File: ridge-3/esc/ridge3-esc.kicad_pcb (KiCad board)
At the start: 6 copper layers, 36 x 36 mm, 202 parts, among them Q1AH TPN2R304PL, Q1AL TPN2R304PL, Q1BH TPN2R304PL, Q1BL TPN2R304PL, Q1CH TPN2R304PL, Q1CL TPN2R304PL, Q2AH TPN2R304PL, Q2AL TPN2R304PL, Q2BH TPN2R304PL, Q2BL TPN2R304PL, Q2CH TPN2R304PL, Q2CL TPN2R304PL, Q3AH TPN2R304PL, Q3AL TPN2R304PL, Q3BH TPN2R304PL, Q3BL TPN2R304PL, Q3CH TPN2R304PL, Q3CL TPN2R304PL, Q4AH TPN2R304PL, Q4AL TPN2R304PL, Q4BH TPN2R304PL, Q4BL TPN2R304PL, Q4CH TPN2R304PL, Q4CL TPN2R304PL

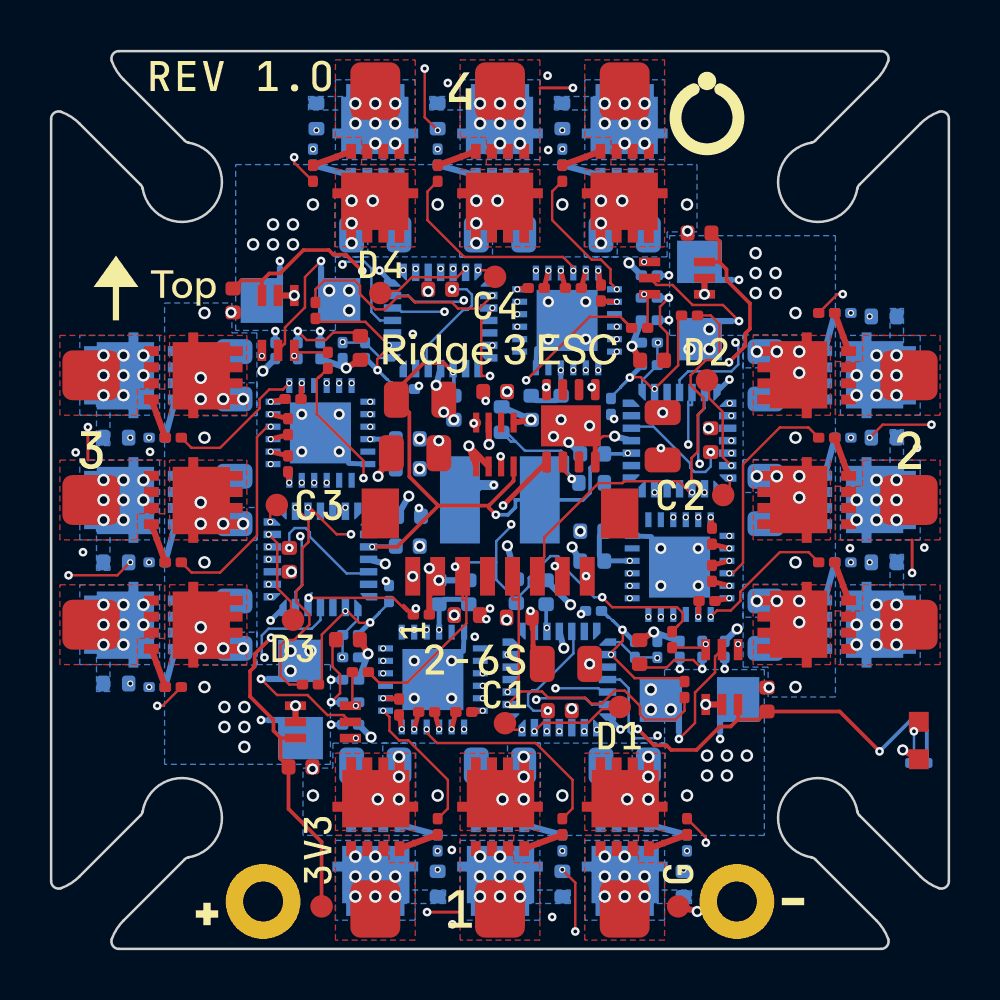
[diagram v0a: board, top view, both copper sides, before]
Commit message: ESC rev 2 routed to DRC 0/0/0 and installed
make.py --reroute esc, every gate passed: DRC 0 errors, 0 warnings,
0 unconnected; copper matches circuit.py pad for pad; BOM and CPL list
exactly the 154 assembled parts; 187 footprints == circuit.py.  8 layers
(In5/In6 gerbers new), 722 pads in the netlist.

Template channel routed with nothing open on every Freerouting variant
tried, 976 of 976 copies stamped onto the four channels, the whole-board
stage's last 4 connections repaired, clean-up from 68 dangling stubs to 0.

Co-Authored-By: Claude Opus 5.5 <noreply@anthropic.com>
Claude-Session: https://claude.ai/code/session_01MaVFAzoExts7u2gmCraXFC
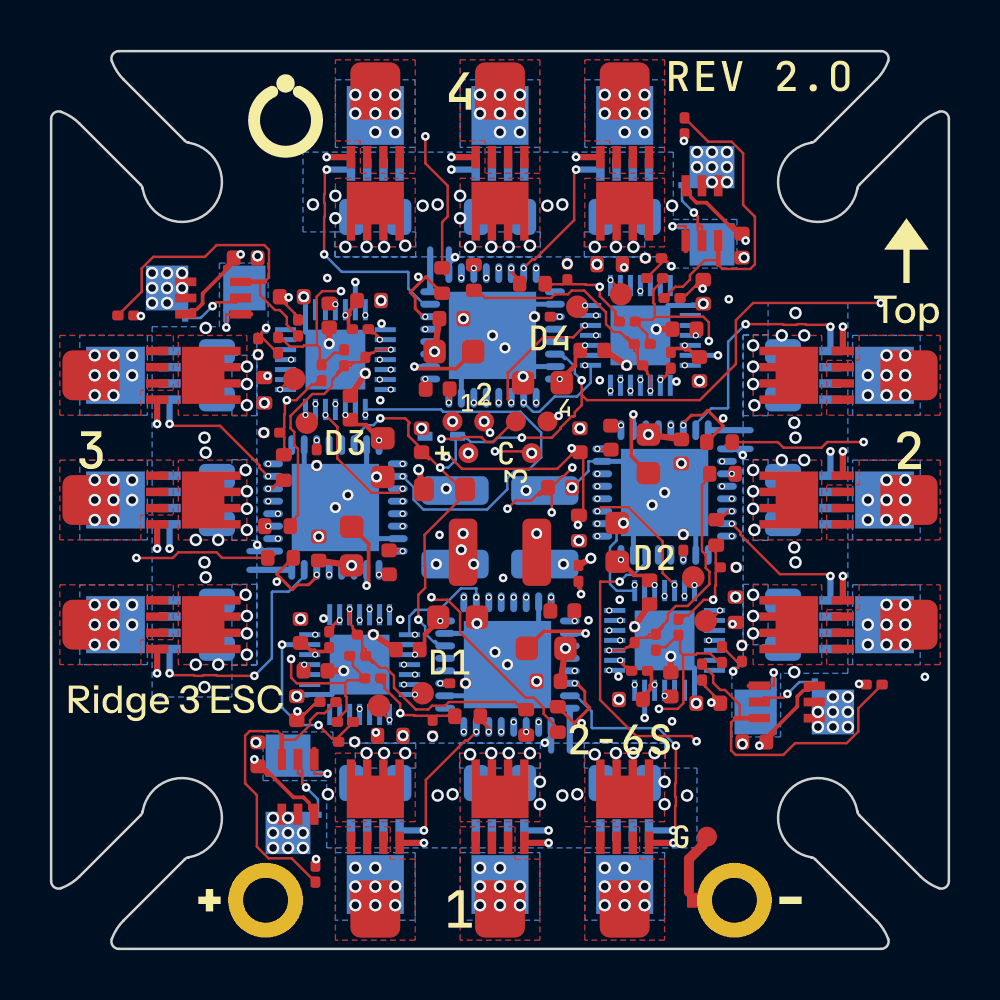
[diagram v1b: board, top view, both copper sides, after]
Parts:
- removed C55: 100nF, C_0402_1005Metric
- removed J_FC: SH-8P V, CONN-TH_BM08B-SRSS-TB-LF-SN
- removed L1: 33uH, IND-SMD_L4.0-W4.0
- removed LED_PWR: RED, LED0603-RD
- removed the P_BAT- at (109.5, 116.1)
- removed the Q1AH at (95.0, 112.3)
- removed the Q1AL at (95.0, 114.7)
- removed the Q1BH at (100.0, 112.3)
- removed the Q1BL at (100.0, 114.7)
- removed the Q1CH at (105.0, 112.3)
- removed the Q1CL at (105.0, 114.7)
- removed the Q2AH at (112.3, 105.0)
- removed the Q2AL at (114.7, 105.0)
- removed the Q2BH at (112.3, 100.0)
- removed the Q2BL at (114.7, 100.0)
- removed the Q2CH at (112.3, 95.0)
- removed the Q2CL at (114.7, 95.0)
- removed the Q3AH at (87.7, 95.0)
- removed the Q3AL at (85.3, 95.0)
- removed the Q3BH at (87.7, 100.0)
- removed the Q3BL at (85.3, 100.0)
- removed the Q3CH at (87.7, 105.0)
- removed the Q3CL at (85.3, 105.0)
- removed the Q4AH at (105.0, 87.7)
- removed the Q4AL at (105.0, 85.3)
- removed the Q4BH at (100.0, 87.7)
- removed the Q4BL at (100.0, 85.3)
- removed the Q4CH at (95.0, 87.7)
- removed the Q4CL at (95.0, 85.3)
- removed R56, R62, R67, R72: 2k, R_0201_0603Metric
- removed R57, R63, R68, R73: 10k, R_0201_0603Metric
- removed R58, R74: 1k, R_0201_0603Metric
- removed R59, R60, R64, R65, R69, R70: 10R, R_0201_0603Metric
- removed R61, R66, R71: 20k, R_0402_1005Metric
- removed TP_3V3, TP_GND: PAD_TP, PAD_TP
- removed U_BUCK: MAX15062A 3.3V, TDFN-8_L2.0-W2.0-P0.50-BL_MAX15062AATA
- removed U_GVDD: TPS7A1601, VSON-8-1EP_3x3mm_P0.65mm_EP1.65x2.4mm
- added D_EN: 4.7V, SOD-523_L1.2-W0.8-LS1.6-RD, B.Cu at (97.6, 97.4)
- added P_BAT-: PAD_BAT_K, PAD_BAT_K, F.Cu at (109.4, 116.0)
- added P_L1: PAD_LEAD, PAD_LEAD, F.Cu at (98.1, 96.8)
- added P_L2: PAD_LEAD, PAD_LEAD, F.Cu at (99.4, 96.8)
- added P_L3: PAD_LEAD, PAD_LEAD, F.Cu at (100.6, 96.8)
- added P_L4: PAD_LEAD, PAD_LEAD, F.Cu at (101.9, 96.8)
- added P_LC: PAD_LEAD, PAD_LEAD, F.Cu at (101.3, 98.1)
- added P_LG: PAD_LEAD, PAD_LEAD, F.Cu at (108.3, 113.5)
- added P_LV: PAD_LEAD, PAD_LEAD, F.Cu at (98.7, 98.1)
- added Q1AH: ISZ023N06LM6, TSDSON-8FL_L3.3-W3.3-P0.65_IFX, F.Cu at (105.0, 112.3)
- added Q1AL: ISZ023N06LM6, TSDSON-8FL_L3.3-W3.3-P0.65_IFX, B.Cu at (105.0, 114.7)
- added Q1BH: ISZ023N06LM6, TSDSON-8FL_L3.3-W3.3-P0.65_IFX, F.Cu at (100.0, 112.3)
- added Q1BL: ISZ023N06LM6, TSDSON-8FL_L3.3-W3.3-P0.65_IFX, B.Cu at (100.0, 114.7)
- added Q1CH: ISZ023N06LM6, TSDSON-8FL_L3.3-W3.3-P0.65_IFX, F.Cu at (95.0, 112.3)
- added Q1CL: ISZ023N06LM6, TSDSON-8FL_L3.3-W3.3-P0.65_IFX, B.Cu at (95.0, 114.7)
- added Q2AH: ISZ023N06LM6, TSDSON-8FL_L3.3-W3.3-P0.65_IFX, F.Cu at (112.3, 95.0)
- added Q2AL: ISZ023N06LM6, TSDSON-8FL_L3.3-W3.3-P0.65_IFX, B.Cu at (114.7, 95.0)
- added Q2BH: ISZ023N06LM6, TSDSON-8FL_L3.3-W3.3-P0.65_IFX, F.Cu at (112.3, 100.0)
- added Q2BL: ISZ023N06LM6, TSDSON-8FL_L3.3-W3.3-P0.65_IFX, B.Cu at (114.7, 100.0)
- added Q2CH: ISZ023N06LM6, TSDSON-8FL_L3.3-W3.3-P0.65_IFX, F.Cu at (112.3, 105.0)
- added Q2CL: ISZ023N06LM6, TSDSON-8FL_L3.3-W3.3-P0.65_IFX, B.Cu at (114.7, 105.0)
- added Q3AH: ISZ023N06LM6, TSDSON-8FL_L3.3-W3.3-P0.65_IFX, F.Cu at (87.7, 105.0)
- added Q3AL: ISZ023N06LM6, TSDSON-8FL_L3.3-W3.3-P0.65_IFX, B.Cu at (85.3, 105.0)
- added Q3BH: ISZ023N06LM6, TSDSON-8FL_L3.3-W3.3-P0.65_IFX, F.Cu at (87.7, 100.0)
- added Q3BL: ISZ023N06LM6, TSDSON-8FL_L3.3-W3.3-P0.65_IFX, B.Cu at (85.3, 100.0)
- added Q3CH: ISZ023N06LM6, TSDSON-8FL_L3.3-W3.3-P0.65_IFX, F.Cu at (87.7, 95.0)
- added Q3CL: ISZ023N06LM6, TSDSON-8FL_L3.3-W3.3-P0.65_IFX, B.Cu at (85.3, 95.0)
- added Q4AH: ISZ023N06LM6, TSDSON-8FL_L3.3-W3.3-P0.65_IFX, F.Cu at (95.0, 87.7)
- added Q4AL: ISZ023N06LM6, TSDSON-8FL_L3.3-W3.3-P0.65_IFX, B.Cu at (95.0, 85.3)
- added Q4BH: ISZ023N06LM6, TSDSON-8FL_L3.3-W3.3-P0.65_IFX, F.Cu at (100.0, 87.7)
- added Q4BL: ISZ023N06LM6, TSDSON-8FL_L3.3-W3.3-P0.65_IFX, B.Cu at (100.0, 85.3)
- added Q4CH: ISZ023N06LM6, TSDSON-8FL_L3.3-W3.3-P0.65_IFX, F.Cu at (105.0, 87.7)
- added Q4CL: ISZ023N06LM6, TSDSON-8FL_L3.3-W3.3-P0.65_IFX, B.Cu at (105.0, 85.3)
- added RT1: NTC 10k B3380, R_0402_1005Metric, F.Cu at (95.6, 109.5)
- added RT2: NTC 10k B3380, R_0402_1005Metric, F.Cu at (109.5, 104.4)
- added RT3: NTC 10k B3380, R_0402_1005Metric, F.Cu at (90.5, 95.6)
- added RT4: NTC 10k B3380, R_0402_1005Metric, F.Cu at (104.4, 90.5)
- C1: value 100nF -> 10uF; footprint C_0402_1005Metric -> C_1210_3225Metric; moved to F.Cu
- C10, C22, C34, C46: value 1uF -> 100nF; moved to F.Cu
- C11, C23, C35, C47: value 100nF -> 1uF; footprint C_0402_1005Metric -> C_0603_1608Metric; moved to F.Cu
- C12, C24, C36, C48: value 1uF -> 47nF; footprint C_0201_0603Metric -> C_0402_1005Metric
- C13, C25, C37, C49: value 4.7uF -> 1uF; footprint C_0805_2012Metric -> C_0603_1608Metric; moved to F.Cu
- C14, C16, C26, C28, C38, C40, C50, C52: value 1uF -> 4.7uF; footprint C_0201_0603Metric -> C_0805_2012Metric; moved to B.Cu
- C17, C29, C41, C53: value 4.7uF -> 100nF; footprint C_0805_2012Metric -> C_0402_1005Metric; moved to F.Cu
- C2: value 1uF -> 10uF; footprint C_0805_2012Metric -> C_1210_3225Metric; moved to B.Cu
- C20, C32, C44, C7, C8, R13, R14, R15, R34, R35: moved to F.Cu
- C3: value 1uF -> 10uF; footprint C_0402_1005Metric -> C_1210_3225Metric; moved to B.Cu
- C4: value 10uF -> 100nF; footprint C_0805_2012Metric -> C_0402_1005Metric
- C5: value 1uF -> 100nF; footprint C_0805_2012Metric -> C_0402_1005Metric
- C6: value 4.7uF -> 100nF; footprint C_0805_2012Metric -> C_0402_1005Metric
- R10, R52: value 10k -> 20k; footprint R_0201_0603Metric -> R_0402_1005Metric
- R11, R53: value 10R -> 2k
- R12, R44, R54: value 10R -> 10k; moved to F.Cu
- R16, R37: value 10R -> 20k; footprint R_0201_0603Metric -> R_0402_1005Metric
- R17, R38: value 10R -> 2k; moved to F.Cu
- R18, R39: value 20k -> 10k; footprint R_0402_1005Metric -> R_0201_0603Metric; moved to F.Cu
- R19: value 2k -> 1k; moved to F.Cu
- R21: value 10R -> 75k
- R22, R28, R49: value 10R -> 20k; footprint R_0201_0603Metric -> R_0402_1005Metric; moved to F.Cu
- R23, R29, R50: value 20k -> 2k; footprint R_0402_1005Metric -> R_0201_0603Metric; moved to F.Cu
- R24, R30, R51: value 2k -> 10k; moved to F.Cu
- R25: value 10k -> 20k; footprint R_0201_0603Metric -> R_0402_1005Metric; moved to F.Cu
- R26: value 1k -> 2k; moved to F.Cu
- R27, R32, R48: value 10R -> 10k
- R31: value 10k -> 1k; moved to F.Cu
- R33: value 10R -> 75k; moved to F.Cu
- R40, R46: value 2k -> 20k; footprint R_0201_0603Metric -> R_0402_1005Metric; moved to F.Cu
- R41, R47: value 10k -> 2k; moved to F.Cu
- R42: value 1k -> 10k; moved to F.Cu
- R43: value 10R -> 1k
- R45: value 20k -> 75k; footprint R_0402_1005Metric -> R_0201_0603Metric; moved to F.Cu
- R5: value 1k -> 33k; footprint R_0201_0603Metric -> R_0603_1608Metric; moved to F.Cu
- R55: value 20k -> 1k; footprint R_0402_1005Metric -> R_0201_0603Metric; moved to F.Cu
- R6: value 22R -> 100k
- R7: value 88.7k -> 10k; footprint R_0402_1005Metric -> R_0201_0603Metric; moved to F.Cu
- R8: value 10.2k -> 10k; footprint R_0402_1005Metric -> R_0201_0603Metric; moved to F.Cu
- R9: value 100k -> 75k; footprint R_0402_1005Metric -> R_0201_0603Metric
- U_ESC1, U_ESC2, U_ESC3, U_ESC4: value STM32G071GBU6 -> AT32F421G8U7; footprint UFQFPN-28_L4.0-W4.0-P0.50-BL -> QFN-28_L4.0-W4.0-P0.40-TL-EP2.4
- U_GD1, U_GD2, U_GD3, U_GD4: value DRV8300DRGER -> DRV8320H; footprint VQFN-24_L4.0-W4.0-P0.50-TL-EP2.5 -> QFN-32_L5.0-W5.0-P0.50-TL-EP3.5
- moved R55 27.1 mm to (106.9, 91.9)
- moved R34 24.7 mm to (91.2, 102.3)
- moved R54 23.9 mm to (105.1, 92.8)
- moved R37 23.6 mm to (91.1, 101.0)
- moved R53 23.0 mm to (102.7, 90.8), turned to 90 degrees
- moved R48 22.4 mm to (106.2, 91.1), turned to 0 degrees
- moved R50 22.2 mm to (105.4, 94.6), turned to 180 degrees
- moved R5 22.0 mm to (97.8, 99.6), turned to 0 degrees
- moved R39 21.7 mm to (93.8, 94.3), turned to 90 degrees
- moved R33 21.1 mm to (92.7, 98.3), turned to -90 degrees
- moved R44 20.8 mm to (106.8, 94.4), turned to -90 degrees
- moved R38 19.3 mm to (94.6, 94.6), turned to -90 degrees
- moved R51 19.2 mm to (105.7, 93.8)
- moved R32 19.2 mm to (94.4, 93.2)
- moved C18 18.9 mm to (91.8, 108.3)
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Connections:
- C1 pad 1: CUR -> VBAT
- C10 pad 1: GVDD -> VBAT
- C11 pad 1: GVDD -> M1_VCP
- C11 pad 2: GND -> VBAT
- C12 pad 1: M1_BSTA -> M1_CPH
- C12 pad 2: M1_A -> M1_CPL
- C13 pad 1: VBAT -> M1_DVDD
- C13 pad 2: M1_SRC -> GND
- C14 pad 1: M1_BSTB -> VBAT
- C14 pad 2: M1_B -> M1_SRC
- C16 pad 1: M1_BSTC -> VBAT
- C16 pad 2: M1_C -> M1_SRC
- C17 pad 1: VBAT -> M1_DVDD
- C17 pad 2: M1_SRC -> GND
- C18 pad 1: +3V3 -> M1_ISENSE
- C19 pad 1: M1_ISENSE -> M2_DVDD
- C20 pad 1: +3V3 -> M2_DVDD
- C22 pad 1: GVDD -> VBAT
- C23 pad 1: GVDD -> M2_VCP
- C23 pad 2: GND -> VBAT
- C24 pad 1: M2_BSTA -> M2_CPH
- C24 pad 2: M2_A -> M2_CPL
- C25 pad 1: VBAT -> M2_DVDD
- C25 pad 2: M2_SRC -> GND
- C26 pad 1: M2_BSTB -> VBAT
- C26 pad 2: M2_B -> M2_SRC
- C28 pad 1: M2_BSTC -> VBAT
- C28 pad 2: M2_C -> M2_SRC
- C29 pad 1: VBAT -> M2_DVDD
- C29 pad 2: M2_SRC -> GND
- C3 pad 1: BUCK_VCC -> VBAT
- C30 pad 1: +3V3 -> M2_ISENSE
- C31 pad 1: M2_ISENSE -> M3_DVDD
- C32 pad 1: +3V3 -> M3_DVDD
- C34 pad 1: GVDD -> VBAT
- C35 pad 1: GVDD -> M3_VCP
- C35 pad 2: GND -> VBAT
- C36 pad 1: M3_BSTA -> M3_CPH
- C36 pad 2: M3_A -> M3_CPL
- C37 pad 1: VBAT -> M3_DVDD
- C37 pad 2: M3_SRC -> GND
- C38 pad 1: M3_BSTB -> VBAT
- C38 pad 2: M3_B -> M3_SRC
- C4 pad 1: +3V3 -> CUR
- C40 pad 1: M3_BSTC -> VBAT
- C40 pad 2: M3_C -> M3_SRC
- C41 pad 1: VBAT -> M3_DVDD
- C41 pad 2: M3_SRC -> GND
- C42 pad 1: +3V3 -> M3_ISENSE
- C43 pad 1: M3_ISENSE -> M4_DVDD
- C44 pad 1: +3V3 -> M4_DVDD
- C46 pad 1: GVDD -> VBAT
- C47 pad 1: GVDD -> M4_VCP
- C47 pad 2: GND -> VBAT
- C48 pad 1: M4_BSTA -> M4_CPH
- C48 pad 2: M4_A -> M4_CPL
- C49 pad 1: VBAT -> M4_DVDD
- C49 pad 2: M4_SRC -> GND
- C5 pad 1: GVDD_IN -> DRV_EN
- C50 pad 1: M4_BSTB -> VBAT
- C50 pad 2: M4_B -> M4_SRC
- C52 pad 1: M4_BSTC -> VBAT
- C52 pad 2: M4_C -> M4_SRC
- C53 pad 1: VBAT -> M4_DVDD
- C53 pad 2: M4_SRC -> GND
- C54 pad 1: +3V3 -> M4_ISENSE
- C6 pad 1: GVDD -> ESC_VSENSE
- C7 pad 1: ESC_VSENSE -> M1_DVDD
- C8 pad 1: +3V3 -> M1_DVDD
- R10 pad 1: ESC_VSENSE -> M1_A
- R10 pad 2: GND -> M1_CMP_A
- R11 pad 1: M1_GHA_D -> M1_CMP_A
- R11 pad 2: M1_GHA -> GND
- R12 pad 1: M1_GLA_D -> M1_CMP_A
- R12 pad 2: M1_GLA -> M1_NEUTRAL
- R13 pad 1: M1_A -> M1_B
- R13 pad 2: M1_CMP_A -> M1_CMP_B
- R14 pad 1: M1_CMP_A -> M1_CMP_B
- R15 pad 1: M1_CMP_A -> M1_CMP_B
- R16 pad 1: M1_GHB_D -> M1_C
- R16 pad 2: M1_GHB -> M1_CMP_C
- R17 pad 1: M1_GLB_D -> M1_CMP_C
- R17 pad 2: M1_GLB -> GND
- R18 pad 1: M1_B -> M1_CMP_C
- R18 pad 2: M1_CMP_B -> M1_NEUTRAL
- R19 pad 1: M1_CMP_B -> M1_IOUT
- R19 pad 2: GND -> M1_ISENSE
- R20 pad 1: M1_CMP_B -> M2_DVDD
- R20 pad 2: M1_NEUTRAL -> M2_NTC
- R21 pad 1: M1_GHC_D -> M2_IDRIVE
- R21 pad 2: M1_GHC -> GND
- R22 pad 1: M1_GLC_D -> M2_A
- R22 pad 2: M1_GLC -> M2_CMP_A
- R23 pad 1: M1_C -> M2_CMP_A
- R23 pad 2: M1_CMP_C -> GND
- R24 pad 1: M1_CMP_C -> M2_CMP_A
- R24 pad 2: GND -> M2_NEUTRAL
- R25 pad 1: M1_CMP_C -> M2_B
- R25 pad 2: M1_NEUTRAL -> M2_CMP_B
- R26 pad 1: M1_IOUT -> M2_CMP_B
- R26 pad 2: M1_ISENSE -> GND
- R27 pad 1: M2_GHA_D -> M2_CMP_B
- R27 pad 2: M2_GHA -> M2_NEUTRAL
- R28 pad 1: M2_GLA_D -> M2_C
- R28 pad 2: M2_GLA -> M2_CMP_C
- R29 pad 1: M2_A -> M2_CMP_C
- R29 pad 2: M2_CMP_A -> GND
- R30 pad 1: M2_CMP_A -> M2_CMP_C
- R30 pad 2: GND -> M2_NEUTRAL
- R31 pad 1: M2_CMP_A -> M2_IOUT
- R31 pad 2: M2_NEUTRAL -> M2_ISENSE
- R32 pad 1: M2_GHB_D -> M3_DVDD
- R32 pad 2: M2_GHB -> M3_NTC
- R33 pad 1: M2_GLB_D -> M3_IDRIVE
- R33 pad 2: M2_GLB -> GND
- R34 pad 1: M2_B -> M3_A
- R34 pad 2: M2_CMP_B -> M3_CMP_A
- R35 pad 1: M2_CMP_B -> M3_CMP_A
- R36 pad 1: M2_CMP_B -> M3_CMP_A
- R36 pad 2: M2_NEUTRAL -> M3_NEUTRAL
- R37 pad 1: M2_GHC_D -> M3_B
- R37 pad 2: M2_GHC -> M3_CMP_B
- R38 pad 1: M2_GLC_D -> M3_CMP_B
- R38 pad 2: M2_GLC -> GND
- R39 pad 1: M2_C -> M3_CMP_B
- R39 pad 2: M2_CMP_C -> M3_NEUTRAL
- R40 pad 1: M2_CMP_C -> M3_C
- R40 pad 2: GND -> M3_CMP_C
- R41 pad 1: M2_CMP_C -> M3_CMP_C
- R41 pad 2: M2_NEUTRAL -> GND
- R42 pad 1: M2_IOUT -> M3_CMP_C
- R42 pad 2: M2_ISENSE -> M3_NEUTRAL
- R43 pad 1: M3_GHA_D -> M3_IOUT
- R43 pad 2: M3_GHA -> M3_ISENSE
- R44 pad 1: M3_GLA_D -> M4_DVDD
- R44 pad 2: M3_GLA -> M4_NTC
- R45 pad 1: M3_A -> M4_IDRIVE
- R45 pad 2: M3_CMP_A -> GND
- R46 pad 1: M3_CMP_A -> M4_A
- R46 pad 2: GND -> M4_CMP_A
- R47 pad 1: M3_CMP_A -> M4_CMP_A
- R47 pad 2: M3_NEUTRAL -> GND
- R48 pad 1: M3_GHB_D -> M4_CMP_A
- R48 pad 2: M3_GHB -> M4_NEUTRAL
- R49 pad 1: M3_GLB_D -> M4_B
- R49 pad 2: M3_GLB -> M4_CMP_B
- R5 pad 1: +3V3 -> VBAT
- R5 pad 2: LED_PWR_A -> DRV_EN
- R50 pad 1: M3_B -> M4_CMP_B
- R50 pad 2: M3_CMP_B -> GND
- R51 pad 1: M3_CMP_B -> M4_CMP_B
- R51 pad 2: GND -> M4_NEUTRAL
- R52 pad 1: M3_CMP_B -> M4_C
- R52 pad 2: M3_NEUTRAL -> M4_CMP_C
- R53 pad 1: M3_GHC_D -> M4_CMP_C
- R53 pad 2: M3_GHC -> GND
- R54 pad 1: M3_GLC_D -> M4_CMP_C
- R54 pad 2: M3_GLC -> M4_NEUTRAL
- R55 pad 1: M3_C -> M4_IOUT
- R55 pad 2: M3_CMP_C -> M4_ISENSE
- R6 pad 2: GVDD_IN -> ESC_VSENSE
- R7 pad 1: GVDD -> ESC_VSENSE
- R7 pad 2: GVDD_FB -> GND
- R8 pad 1: GVDD_FB -> M1_DVDD
- R8 pad 2: GND -> M1_NTC
- R9 pad 1: VBAT -> M1_IDRIVE
- R9 pad 2: ESC_VSENSE -> GND
- U_CS1 pad 3: +3V3 -> M1_DVDD
- U_CS2 pad 3: +3V3 -> M2_DVDD
- U_CS3 pad 3: +3V3 -> M3_DVDD
- U_CS4 pad 3: +3V3 -> M4_DVDD
- U_ESC1 pad 1: (no net) -> GND
- U_ESC1 pad 10: (no net) -> M1_CMP_B
- U_ESC1 pad 11: M1_ISENSE -> M1_CMP_C
- U_ESC1 pad 12: ESC_VSENSE -> M1_ISENSE
- U_ESC1 pad 16: M1_HC -> GND
- U_ESC1 pad 17: (no net) -> M1_DVDD
- U_ESC1 pad 18: M1_HB -> M1_HC
- U_ESC1 pad 19: M1_HA -> M1_HB
- U_ESC1 pad 20: M1_SWDIO -> M1_HA
- U_ESC1 pad 21: M1_SWCLK -> M1_SWDIO
- U_ESC1 pad 22: (no net) -> M1_SWCLK
- U_ESC1 pad 23: M1_CMP_B -> (no net)
- U_ESC1 pad 24: M1_SIG -> (no net)
- U_ESC1 pad 25: (no net) -> M1_SIG
- U_ESC1 pad 27: M1_CMP_A -> (no net)
- U_ESC1 pad 3: +3V3 -> (no net)
- U_ESC1 pad 4: GND -> M1_NRST
- U_ESC1 pad 5: M1_NRST -> M1_DVDD
- U_ESC1 pad 6: (no net) -> M1_CMP_A
- U_ESC1 pad 7: (no net) -> M1_NEUTRAL
- U_ESC1 pad 8: M1_CMP_C -> ESC_VSENSE
- U_ESC1 pad 9: M1_NEUTRAL -> M1_NTC
- U_ESC2 pad 1: (no net) -> GND
- U_ESC2 pad 10: (no net) -> M2_CMP_B
- U_ESC2 pad 11: M2_ISENSE -> M2_CMP_C
- U_ESC2 pad 12: ESC_VSENSE -> M2_ISENSE
- U_ESC2 pad 16: M2_HC -> GND
- U_ESC2 pad 17: (no net) -> M2_DVDD
- U_ESC2 pad 18: M2_HB -> M2_HC
- U_ESC2 pad 19: M2_HA -> M2_HB
- U_ESC2 pad 20: M2_SWDIO -> M2_HA
- U_ESC2 pad 21: M2_SWCLK -> M2_SWDIO
- U_ESC2 pad 22: (no net) -> M2_SWCLK
- U_ESC2 pad 23: M2_CMP_B -> (no net)
- U_ESC2 pad 24: M2_SIG -> (no net)
- U_ESC2 pad 25: (no net) -> M2_SIG
- U_ESC2 pad 27: M2_CMP_A -> (no net)
- U_ESC2 pad 3: +3V3 -> (no net)
- U_ESC2 pad 4: GND -> M2_NRST
- U_ESC2 pad 5: M2_NRST -> M2_DVDD
- U_ESC2 pad 6: (no net) -> M2_CMP_A
- U_ESC2 pad 7: (no net) -> M2_NEUTRAL
- U_ESC2 pad 8: M2_CMP_C -> ESC_VSENSE
- U_ESC2 pad 9: M2_NEUTRAL -> M2_NTC
- U_ESC3 pad 1: (no net) -> GND
- U_ESC3 pad 10: (no net) -> M3_CMP_B
- U_ESC3 pad 11: M3_ISENSE -> M3_CMP_C
- U_ESC3 pad 12: ESC_VSENSE -> M3_ISENSE
- U_ESC3 pad 16: M3_HC -> GND
- U_ESC3 pad 17: (no net) -> M3_DVDD
- U_ESC3 pad 18: M3_HB -> M3_HC
- U_ESC3 pad 19: M3_HA -> M3_HB
- U_ESC3 pad 20: M3_SWDIO -> M3_HA
- U_ESC3 pad 21: M3_SWCLK -> M3_SWDIO
- U_ESC3 pad 22: (no net) -> M3_SWCLK
- U_ESC3 pad 23: M3_CMP_B -> (no net)
- U_ESC3 pad 24: M3_SIG -> (no net)
- U_ESC3 pad 25: (no net) -> M3_SIG
- U_ESC3 pad 27: M3_CMP_A -> (no net)
- U_ESC3 pad 3: +3V3 -> (no net)
- U_ESC3 pad 4: GND -> M3_NRST
- U_ESC3 pad 5: M3_NRST -> M3_DVDD
- U_ESC3 pad 6: (no net) -> M3_CMP_A
- U_ESC3 pad 7: (no net) -> M3_NEUTRAL
- U_ESC3 pad 8: M3_CMP_C -> ESC_VSENSE
- U_ESC3 pad 9: M3_NEUTRAL -> M3_NTC
- U_ESC4 pad 1: (no net) -> GND
- U_ESC4 pad 10: (no net) -> M4_CMP_B
- U_ESC4 pad 11: M4_ISENSE -> M4_CMP_C
- U_ESC4 pad 12: ESC_VSENSE -> M4_ISENSE
- U_ESC4 pad 16: M4_HC -> GND
- U_ESC4 pad 17: (no net) -> M4_DVDD
- U_ESC4 pad 18: M4_HB -> M4_HC
- U_ESC4 pad 19: M4_HA -> M4_HB
- U_ESC4 pad 20: M4_SWDIO -> M4_HA
- U_ESC4 pad 21: M4_SWCLK -> M4_SWDIO
- U_ESC4 pad 22: (no net) -> M4_SWCLK
- U_ESC4 pad 23: M4_CMP_B -> (no net)
- U_ESC4 pad 24: M4_SIG -> (no net)
- U_ESC4 pad 25: (no net) -> M4_SIG
- U_ESC4 pad 27: M4_CMP_A -> (no net)
- U_ESC4 pad 3: +3V3 -> (no net)
- U_ESC4 pad 4: GND -> M4_NRST
- U_ESC4 pad 5: M4_NRST -> M4_DVDD
- U_ESC4 pad 6: (no net) -> M4_CMP_A
- U_ESC4 pad 7: (no net) -> M4_NEUTRAL
- U_ESC4 pad 8: M4_CMP_C -> ESC_VSENSE
- U_ESC4 pad 9: M4_NEUTRAL -> M4_NTC
- U_GD1 pad 1: M1_LA -> M1_CPH
- U_GD1 pad 10: M1_GLB_D -> M1_GLB
- U_GD1 pad 11: M1_GLA_D -> M1_B
- U_GD1 pad 12: M1_C -> M1_GHB
- U_GD1 pad 13: M1_GHC_D -> M1_GHC
- U_GD1 pad 14: M1_BSTC -> M1_C
- U_GD1 pad 15: M1_B -> M1_GLC
- U_GD1 pad 16: M1_GHB_D -> M1_SRC
- U_GD1 pad 17: M1_BSTB -> (no net)
- U_GD1 pad 18: M1_A -> GND
- U_GD1 pad 19: M1_GHA_D -> M1_IDRIVE
- U_GD1 pad 2: M1_LB -> M1_VCP
- U_GD1 pad 20: M1_BSTA -> (no net)
- U_GD1 pad 22: M1_HA -> DRV_EN
- U_GD1 pad 23: M1_HB -> GND
- U_GD1 pad 24: M1_HC -> M1_DVDD
- U_GD1 pad 25: GND -> M1_HA
- U_GD1 pad 3: M1_LC -> VBAT
- U_GD1 pad 4: GVDD -> VBAT
- U_GD1 pad 5: (no net) -> M1_GHA
- U_GD1 pad 6: GND -> M1_A
- U_GD1 pad 7: (no net) -> M1_GLA
- U_GD1 pad 8: (no net) -> M1_SRC
- U_GD1 pad 9: M1_GLC_D -> M1_SRC
- U_GD2 pad 1: M2_LA -> M2_CPH
- U_GD2 pad 10: M2_GLB_D -> M2_GLB
- U_GD2 pad 11: M2_GLA_D -> M2_B
- U_GD2 pad 12: M2_C -> M2_GHB
- U_GD2 pad 13: M2_GHC_D -> M2_GHC
- U_GD2 pad 14: M2_BSTC -> M2_C
- U_GD2 pad 15: M2_B -> M2_GLC
- U_GD2 pad 16: M2_GHB_D -> M2_SRC
- U_GD2 pad 17: M2_BSTB -> (no net)
- U_GD2 pad 18: M2_A -> GND
- U_GD2 pad 19: M2_GHA_D -> M2_IDRIVE
- U_GD2 pad 2: M2_LB -> M2_VCP
- U_GD2 pad 20: M2_BSTA -> (no net)
- U_GD2 pad 22: M2_HA -> DRV_EN
- U_GD2 pad 23: M2_HB -> GND
- U_GD2 pad 24: M2_HC -> M2_DVDD
- U_GD2 pad 25: GND -> M2_HA
- U_GD2 pad 3: M2_LC -> VBAT
- U_GD2 pad 4: GVDD -> VBAT
- U_GD2 pad 5: (no net) -> M2_GHA
- U_GD2 pad 6: GND -> M2_A
- U_GD2 pad 7: (no net) -> M2_GLA
- U_GD2 pad 8: (no net) -> M2_SRC
- U_GD2 pad 9: M2_GLC_D -> M2_SRC
- U_GD3 pad 1: M3_LA -> M3_CPH
- U_GD3 pad 10: M3_GLB_D -> M3_GLB
- U_GD3 pad 11: M3_GLA_D -> M3_B
- U_GD3 pad 12: M3_C -> M3_GHB
- U_GD3 pad 13: M3_GHC_D -> M3_GHC
- U_GD3 pad 14: M3_BSTC -> M3_C
- U_GD3 pad 15: M3_B -> M3_GLC
- U_GD3 pad 16: M3_GHB_D -> M3_SRC
- U_GD3 pad 17: M3_BSTB -> (no net)
- U_GD3 pad 18: M3_A -> GND
- U_GD3 pad 19: M3_GHA_D -> M3_IDRIVE
- U_GD3 pad 2: M3_LB -> M3_VCP
- U_GD3 pad 20: M3_BSTA -> (no net)
- U_GD3 pad 22: M3_HA -> DRV_EN
- U_GD3 pad 23: M3_HB -> GND
- U_GD3 pad 24: M3_HC -> M3_DVDD
- U_GD3 pad 25: GND -> M3_HA
- U_GD3 pad 3: M3_LC -> VBAT
- U_GD3 pad 4: GVDD -> VBAT
- U_GD3 pad 5: (no net) -> M3_GHA
- U_GD3 pad 6: GND -> M3_A
- U_GD3 pad 7: (no net) -> M3_GLA
- U_GD3 pad 8: (no net) -> M3_SRC
- U_GD3 pad 9: M3_GLC_D -> M3_SRC
- U_GD4 pad 1: M4_LA -> M4_CPH
- U_GD4 pad 10: M4_GLB_D -> M4_GLB
- U_GD4 pad 11: M4_GLA_D -> M4_B
- U_GD4 pad 12: M4_C -> M4_GHB
- U_GD4 pad 13: M4_GHC_D -> M4_GHC
- U_GD4 pad 14: M4_BSTC -> M4_C
- U_GD4 pad 15: M4_B -> M4_GLC
- U_GD4 pad 16: M4_GHB_D -> M4_SRC
- U_GD4 pad 17: M4_BSTB -> (no net)
- U_GD4 pad 18: M4_A -> GND
- U_GD4 pad 19: M4_GHA_D -> M4_IDRIVE
- U_GD4 pad 2: M4_LB -> M4_VCP
- U_GD4 pad 20: M4_BSTA -> (no net)
- U_GD4 pad 22: M4_HA -> DRV_EN
- U_GD4 pad 23: M4_HB -> GND
- U_GD4 pad 24: M4_HC -> M4_DVDD
- U_GD4 pad 25: GND -> M4_HA
- U_GD4 pad 3: M4_LC -> VBAT
- U_GD4 pad 4: GVDD -> VBAT
- U_GD4 pad 5: (no net) -> M4_GHA
- U_GD4 pad 6: GND -> M4_A
- U_GD4 pad 7: (no net) -> M4_GLA
- U_GD4 pad 8: (no net) -> M4_SRC
- U_GD4 pad 9: M4_GLC_D -> M4_SRC
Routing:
- net +3V3: track 103.2 -> 0.00 mm, vias 11 -> 0
- net DRV_EN: track 0.00 -> 77.6 mm, vias 0 -> 9
- net GVDD: track 53.6 -> 0.00 mm, vias 7 -> 0
- net CUR: track 45.4 -> 83.8 mm, vias 5 -> 10
- net M3_CMP_B: track 35.0 -> 10.8 mm, vias 4 -> 1
- net M4_CMP_B: track 35.0 -> 10.8 mm, vias 4 -> 1
- net M1_CMP_B: track 35.0 -> 10.8 mm, vias 4 -> 1
- net M2_CMP_B: track 35.0 -> 10.8 mm, vias 4 -> 1
- net M4_DVDD: track 0.00 -> 19.5 mm, vias 0 -> 4
- net M3_DVDD: track 0.00 -> 19.5 mm, vias 0 -> 4
- net M2_DVDD: track 0.00 -> 19.5 mm, vias 0 -> 4
- net M1_DVDD: track 0.00 -> 19.5 mm, vias 0 -> 4
- net M2_GHC_D: track 18.5 -> 0.00 mm, vias 3 -> 0
- net M1_GHC_D: track 18.5 -> 0.00 mm, vias 3 -> 0
- net M4_GHC_D: track 18.5 -> 0.00 mm, vias 3 -> 0
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- added copper zone on In4.Cu, net GND
- added copper zone on In5.Cu, net M1_SRC
- added copper zone on In5.Cu, net M2_SRC
- added copper zone on In5.Cu, net M3_SRC
- added copper zone on In5.Cu, net M4_SRC
- added copper zone on In3.Cu, net VBAT
- added copper zone on In6.Cu, net VBAT
- removed copper zone on In3.Cu, net M1_SRC
- removed copper zone on In3.Cu, net M2_SRC
- removed copper zone on In3.Cu, net M3_SRC
- removed copper zone on In3.Cu, net M4_SRC
- removed copper zone on In4.Cu, net VBAT
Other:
- copper layers 6 -> 8

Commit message: ESC rebuilt: each channel's MCU on the FC's 3.3 V, routed to DRC 0
The four channels' 3.3 V from the stack lead's pin 4 (ESC_3V3) through each
channel's 0201 bead at the mouth of its way into the middle; DRC 0 errors,
0 warnings, 0 unconnected; copper matches circuit.py pad for pad; 159
assembled parts in the BOM and CPL.

cleanup.py: the passes repeat while one keeps an edit and dangling copper is
left (a trim had left a stub lying along its own net's track, which the next
pass takes away).

esc_layout.py: an SWD clock pad whose 'Cn' finds no room takes the letter
alone (its data pad beside it carries the channel's number); applied with
the next artwork run.

Co-Authored-By: Claude Opus 5.5 <noreply@anthropic.com>
Claude-Session: https://claude.ai/code/session_01MaVFAzoExts7u2gmCraXFC
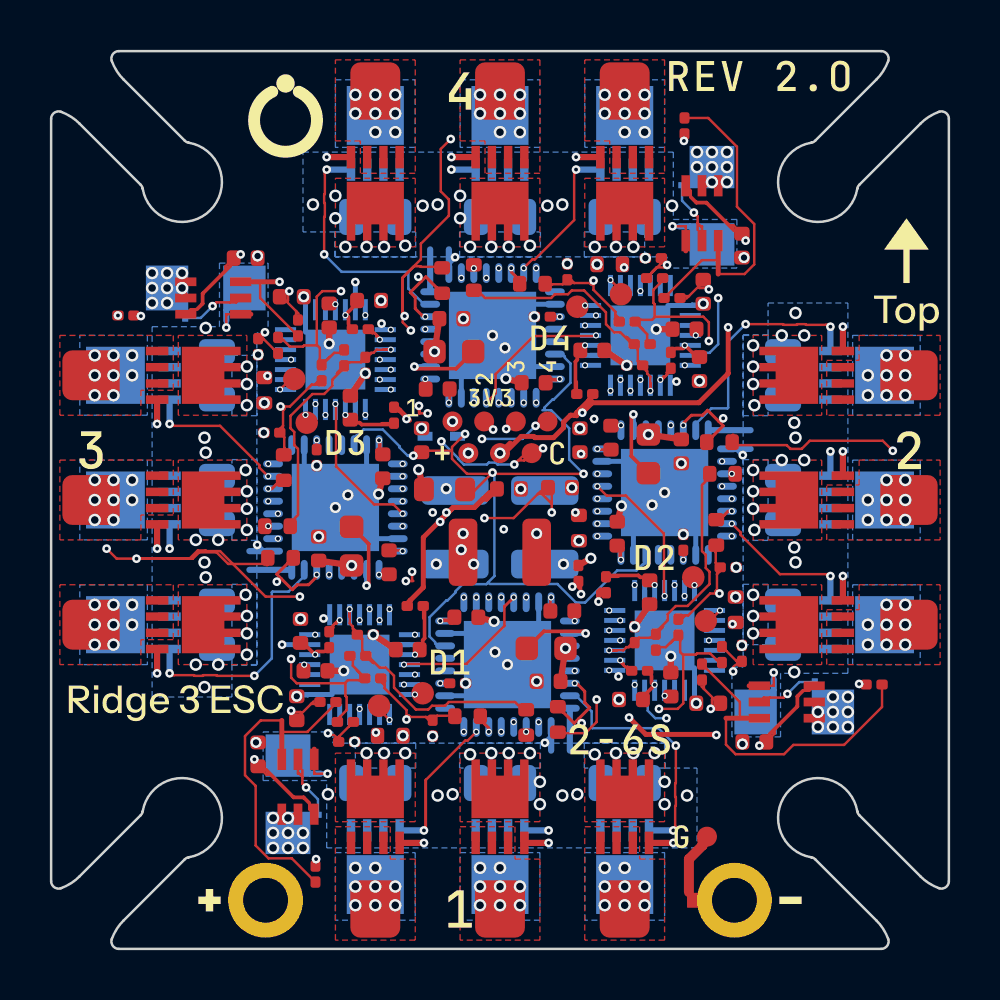
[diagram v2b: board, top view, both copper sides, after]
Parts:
- added C55: 100nF, C_0402_1005Metric, F.Cu at (108.2, 91.7)
- added FB1: 600R@100MHz, L_0201_0603Metric, F.Cu at (96.6, 104.2)
- added FB2: 600R@100MHz, L_0201_0603Metric, F.Cu at (104.2, 103.4)
- added FB3: 600R@100MHz, L_0201_0603Metric, F.Cu at (95.8, 96.6)
- added FB4: 600R@100MHz, L_0201_0603Metric, F.Cu at (103.4, 95.8)
- added P_L3V: PAD_LEAD, PAD_LEAD, F.Cu at (100.0, 98.1)
- C11, C23, C35, C47: value 1uF -> 100nF; footprint C_0603_1608Metric -> C_0402_1005Metric
- C12, C24, C36, C48: value 47nF -> 1uF; footprint C_0402_1005Metric -> C_0603_1608Metric
- C13, C25, C37, C49: value 1uF -> 47nF; footprint C_0603_1608Metric -> C_0402_1005Metric
- C14, C26, C38, C50: value 4.7uF -> 1uF; footprint C_0805_2012Metric -> C_0402_1005Metric; moved to F.Cu
- C17, C29, C41, C53: value 100nF -> 4.7uF; footprint C_0402_1005Metric -> C_0805_2012Metric; moved to B.Cu
- C21, C33, C45, C9: value 100nF -> 1uF
- moved C31 18.6 mm to (108.3, 108.2), turned to 180 degrees
- moved C19 14.9 mm to (91.8, 108.3), turned to 90 degrees
- moved C43 12.2 mm to (91.7, 91.8)
- moved C7 10.9 mm to (103.2, 97.6), turned to 90 degrees
- moved C10 9.36 mm to (92.6, 106.8), turned to 0 degrees
- moved C22 9.36 mm to (106.8, 107.4), turned to 90 degrees
- moved C34 9.36 mm to (93.2, 92.6), turned to -90 degrees
- moved C46 9.36 mm to (107.4, 93.2), turned to 180 degrees
- moved C14 9.19 mm to (98.7, 104.7)
- moved C26 9.19 mm to (104.7, 101.3)
- moved C38 9.19 mm to (95.3, 98.7)
- moved C50 9.19 mm to (101.3, 95.3)
- moved C6 6.35 mm to (96.9, 97.6)
- moved C15 5.00 mm to (105.0, 111.3)
- moved C16 5.00 mm to (100.0, 111.3), turned to 0 degrees
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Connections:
- C10 pad 1: VBAT -> M1_NRST
- C11 pad 1: M1_VCP -> VBAT
- C11 pad 2: VBAT -> GND
- C12 pad 1: M1_CPH -> M1_VCP
- C12 pad 2: M1_CPL -> VBAT
- C13 pad 1: M1_DVDD -> M1_CPH
- C13 pad 2: GND -> M1_CPL
- C14 pad 1: VBAT -> M1_DVDD
- C14 pad 2: M1_SRC -> GND
- C17 pad 1: M1_DVDD -> VBAT
- C17 pad 2: GND -> M1_SRC
- C18 pad 1: M1_ISENSE -> M1_3V3
- C19 pad 1: M2_DVDD -> M1_ISENSE
- C20 pad 1: M2_DVDD -> M2_3V3
- C21 pad 1: M2_NRST -> M2_3V3
- C22 pad 1: VBAT -> M2_NRST
- C23 pad 1: M2_VCP -> VBAT
- C23 pad 2: VBAT -> GND
- C24 pad 1: M2_CPH -> M2_VCP
- C24 pad 2: M2_CPL -> VBAT
- C25 pad 1: M2_DVDD -> M2_CPH
- C25 pad 2: GND -> M2_CPL
- C26 pad 1: VBAT -> M2_DVDD
- C26 pad 2: M2_SRC -> GND
- C29 pad 1: M2_DVDD -> VBAT
- C29 pad 2: GND -> M2_SRC
- C30 pad 1: M2_ISENSE -> M2_3V3
- C31 pad 1: M3_DVDD -> M2_ISENSE
- C32 pad 1: M3_DVDD -> M3_3V3
- C33 pad 1: M3_NRST -> M3_3V3
- C34 pad 1: VBAT -> M3_NRST
- C35 pad 1: M3_VCP -> VBAT
- C35 pad 2: VBAT -> GND
- C36 pad 1: M3_CPH -> M3_VCP
- C36 pad 2: M3_CPL -> VBAT
- C37 pad 1: M3_DVDD -> M3_CPH
- C37 pad 2: GND -> M3_CPL
- C38 pad 1: VBAT -> M3_DVDD
- C38 pad 2: M3_SRC -> GND
- C41 pad 1: M3_DVDD -> VBAT
- C41 pad 2: GND -> M3_SRC
- C42 pad 1: M3_ISENSE -> M3_3V3
- C43 pad 1: M4_DVDD -> M3_ISENSE
- C44 pad 1: M4_DVDD -> M4_3V3
- C45 pad 1: M4_NRST -> M4_3V3
- C46 pad 1: VBAT -> M4_NRST
- C47 pad 1: M4_VCP -> VBAT
- C47 pad 2: VBAT -> GND
- C48 pad 1: M4_CPH -> M4_VCP
- C48 pad 2: M4_CPL -> VBAT
- C49 pad 1: M4_DVDD -> M4_CPH
- C49 pad 2: GND -> M4_CPL
- C5 pad 1: DRV_EN -> ESC_3V3
- C50 pad 1: VBAT -> M4_DVDD
- C50 pad 2: M4_SRC -> GND
- C53 pad 1: M4_DVDD -> VBAT
- C53 pad 2: GND -> M4_SRC
- C54 pad 1: M4_ISENSE -> M4_3V3
- C6 pad 1: ESC_VSENSE -> DRV_EN
- C7 pad 1: M1_DVDD -> ESC_VSENSE
- C8 pad 1: M1_DVDD -> M1_3V3
- C9 pad 1: M1_NRST -> M1_3V3
- R20 pad 1: M2_DVDD -> M2_3V3
- R32 pad 1: M3_DVDD -> M3_3V3
- R44 pad 1: M4_DVDD -> M4_3V3
- R8 pad 1: M1_DVDD -> M1_3V3
- U_CS1 pad 3: M1_DVDD -> M1_3V3
- U_CS2 pad 3: M2_DVDD -> M2_3V3
- U_CS3 pad 3: M3_DVDD -> M3_3V3
- U_CS4 pad 3: M4_DVDD -> M4_3V3
- U_ESC1 pad 17: M1_DVDD -> M1_3V3
- U_ESC1 pad 5: M1_DVDD -> M1_3V3
- U_ESC2 pad 17: M2_DVDD -> M2_3V3
- U_ESC2 pad 5: M2_DVDD -> M2_3V3
- U_ESC3 pad 17: M3_DVDD -> M3_3V3
- U_ESC3 pad 5: M3_DVDD -> M3_3V3
- U_ESC4 pad 17: M4_DVDD -> M4_3V3
- U_ESC4 pad 5: M4_DVDD -> M4_3V3
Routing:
- net ESC_3V3: track 0.00 -> 85.9 mm, vias 0 -> 9
- net DRV_EN: track 77.6 -> 36.7 mm, vias 9 -> 4
- net M3_CMP_A: track 35.4 -> 73.9 mm, vias 4 -> 5
- net M4_DVDD: track 19.5 -> 0.82 mm, vias 4 -> 1
- net M3_DVDD: track 19.5 -> 0.82 mm, vias 4 -> 1
- net M2_DVDD: track 19.5 -> 0.82 mm, vias 4 -> 1
- net M1_DVDD: track 19.5 -> 0.82 mm, vias 4 -> 1
- net M3_3V3: track 0.00 -> 18.0 mm, vias 0 -> 3
- net M2_3V3: track 0.00 -> 18.0 mm, vias 0 -> 3
- net M1_3V3: track 0.00 -> 18.0 mm, vias 0 -> 3
- net M4_3V3: track 0.00 -> 18.0 mm, vias 0 -> 3
- net M4_LC: track 24.5 -> 7.27 mm
- net M3_LC: track 24.5 -> 7.27 mm
- net M2_LC: track 24.5 -> 7.27 mm
- net M4_CMP_A: track 36.2 -> 53.4 mm, vias 4 -> 5
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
